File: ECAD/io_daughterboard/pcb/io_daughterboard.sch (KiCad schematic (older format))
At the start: 89 parts, among them CON1 BARREL_JACK, J1 XF2L-0625-1A, J2 4-1734839-0, P1 CONN_02X32, P10 CONN_01X06, P11 CONN_01X06, P12 CONN_01X06, P13 CONN_01X06, P14 CONN_01X06, P15 CONN_01X06, P16 CONN_01X06, P17 CONN_01X06, P18 CONN_01X06, P19 CONN_01X04, P2 CONN_02X32, P3 CONN_01X06, P4 CONN_01X06, P5 CONN_01X06, P6 CONN_01X06, P7 CONN_01X06, P8 CONN_01X06, P9 CONN_01X06, SW1 Reset Button, SW2 User Button, U1 FAN5333BSX, U10 SN74LV1T34DCKR, U11 SN74LV1T34DCKR, U2 SPX3819M5-L-3-3, U3 74HC244, U4 74HC244, U5 74HC244, U6 STMPE811QTR, U7 74HC244, U8 74HC244, U9 74HC244

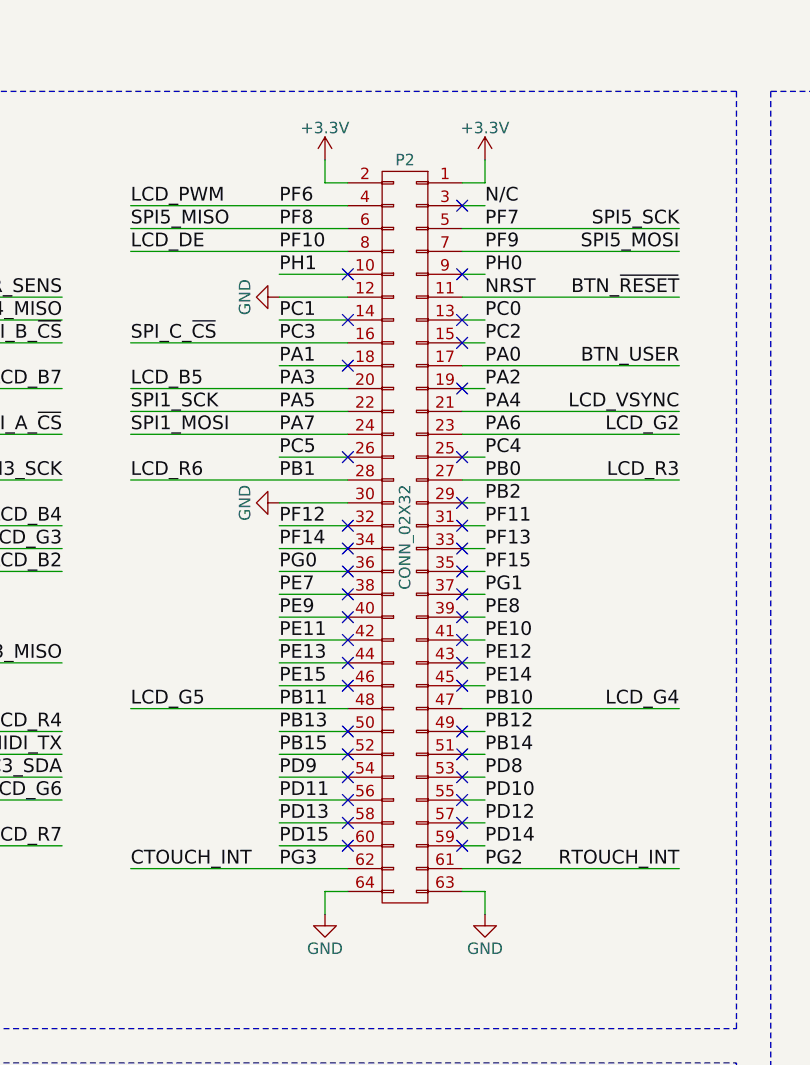
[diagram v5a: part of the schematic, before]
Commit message: Flipped board to make LCD right side up.  Regenerated netlist with footprints.
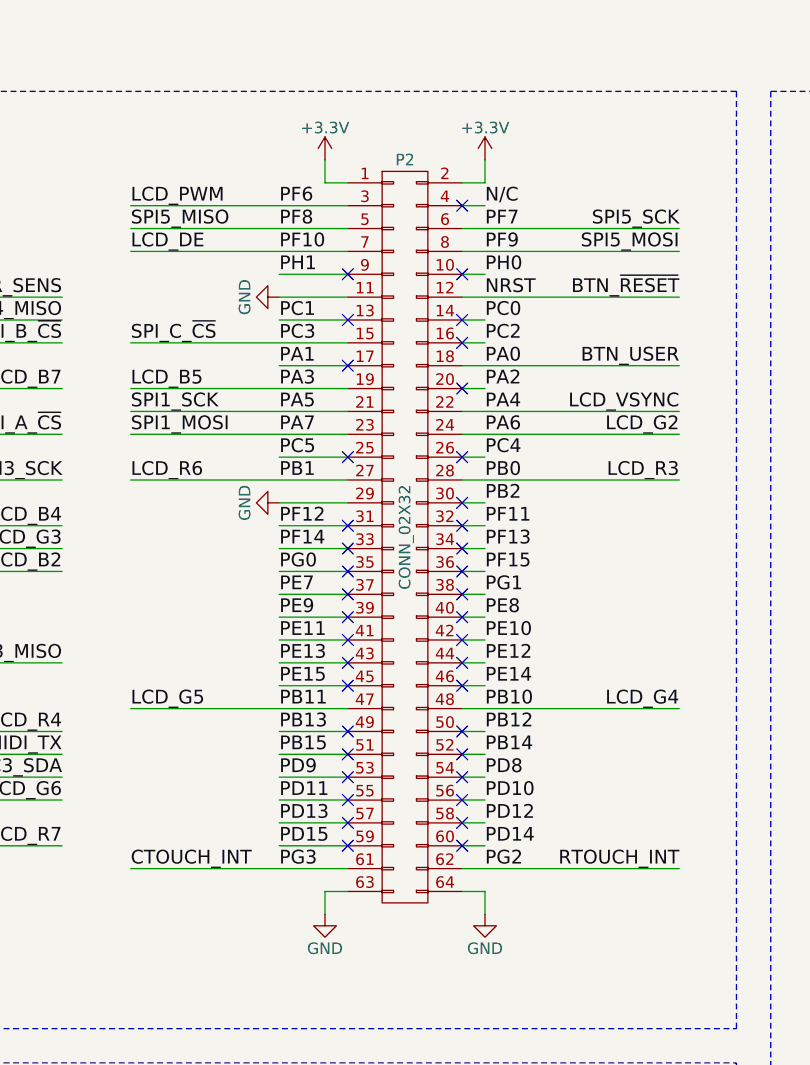
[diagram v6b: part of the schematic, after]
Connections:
- net BTN_USER: now also P2.18 (P18); no longer P2.17 (P17)
- net BTN_~RESET: now also P2.12 (P12); no longer P2.11 (P11)
- net CTOUCH_INT: now also P2.61 (P61); no longer P2.62 (P62)
- net GND: now also P2.11 (P11), P2.29 (P29); no longer P2.12 (P12), P2.30 (P30)
- net LCD_B5: now also P2.19 (P19); no longer P2.20 (P20)
- net LCD_DE: now also P2.7 (P7); no longer P2.8 (P8)
- net LCD_G2: now also P2.24 (P24); no longer P2.23 (P23)
- net LCD_G4: now also P2.48 (P48); no longer P2.47 (P47)
- net LCD_G5: now also P2.47 (P47); no longer P2.48 (P48)
- net LCD_PWM: now also P2.3 (P3); no longer P2.4 (P4)
- net LCD_R0: now also P2.27 (P27); no longer P2.28 (P28)
- net LCD_R3: now also P2.28 (P28); no longer P2.27 (P27)
- net LCD_VSYNC: now also P2.22 (P22); no longer P2.21 (P21)
- net N/C: now also P2.4 (P4); no longer P2.3 (P3)
- net PA1: now also P2.17 (P17); no longer P2.18 (P18)
- net PA2: now also P2.20 (P20); no longer P2.19 (P19)
- net PA5: now also P2.21 (P21); no longer P2.22 (P22)
- net PA7: now also P2.23 (P23); no longer P2.24 (P24)
- net PB12: now also P2.50 (P50); no longer P2.49 (P49)
- net PB13: now also P2.49 (P49); no longer P2.50 (P50)
- net PB14: now also P2.52 (P52); no longer P2.51 (P51)
- net PB15: now also P2.51 (P51); no longer P2.52 (P52)
- net PB2: now also P2.30 (P30); no longer P2.29 (P29)
- net PC0: now also P2.14 (P14); no longer P2.13 (P13)
- net PC1: now also P2.13 (P13); no longer P2.14 (P14)
- net PC2: now also P2.16 (P16); no longer P2.15 (P15)
- net PC3: now also P2.15 (P15); no longer P2.16 (P16)
- net PC4: now also P2.26 (P26); no longer P2.25 (P25)
- net PC5: now also P2.25 (P25); no longer P2.26 (P26)
- net PD10: now also P2.56 (P56); no longer P2.55 (P55)
- net PD11: now also P2.55 (P55); no longer P2.56 (P56)
- net PD12: now also P2.58 (P58); no longer P2.57 (P57)
- net PD13: now also P2.57 (P57); no longer P2.58 (P58)
- net PD14: now also P2.60 (P60); no longer P2.59 (P59)
- net PD15: now also P2.59 (P59); no longer P2.60 (P60)
- net PD8: now also P2.54 (P54); no longer P2.53 (P53)
- net PD9: now also P2.53 (P53); no longer P2.54 (P54)
- net PE10: now also P2.42 (P42); no longer P2.41 (P41)
- net PE11: now also P2.41 (P41); no longer P2.42 (P42)
- net PE12: now also P2.44 (P44); no longer P2.43 (P43)
- net PE13: now also P2.43 (P43); no longer P2.44 (P44)
- net PE14: now also P2.46 (P46); no longer P2.45 (P45)
- net PE15: now also P2.45 (P45); no longer P2.46 (P46)
- net PE7: now also P2.37 (P37); no longer P2.38 (P38)
- net PE8: now also P2.40 (P40); no longer P2.39 (P39)
- net PE9: now also P2.39 (P39); no longer P2.40 (P40)
- net PF11: now also P2.32 (P32); no longer P2.31 (P31)
- net PF12: now also P2.31 (P31); no longer P2.32 (P32)
- net PF13: now also P2.34 (P34); no longer P2.33 (P33)
- net PF14: now also P2.33 (P33); no longer P2.34 (P34)
- net PF15: now also P2.36 (P36); no longer P2.35 (P35)
- net PF7: now also P2.6 (P6); no longer P2.5 (P5)
- net PF8: now also P2.5 (P5); no longer P2.6 (P6)
- net PF9: now also P2.8 (P8); no longer P2.7 (P7)
- net PG0: now also P2.35 (P35); no longer P2.36 (P36)
- net PG1: now also P2.38 (P38); no longer P2.37 (P37)
- net PG2: now also P2.62 (P62); no longer P2.61 (P61)
- net PH0: now also P2.10 (P10); no longer P2.9 (P9)
- net PH1: now also P2.9 (P9); no longer P2.10 (P10)
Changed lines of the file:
@@
 F 3 "" H 4800 2150 50  0000 C CNN
 	1    4800 2550
-	-1   0    0    -1
+	1    0    0    -1
 $EndComp
 $Comp

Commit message: Dimensioned board for P1 and P2 connectors.  Experimenting with different slave connectors.
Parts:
- P1, P2: footprint Socket_Strips:Socket_Strip_Straight_2x32 -> daughterfeet:Socket_Strip_Reversed_2x32
- P10, P11, P12, P13, P14, P15, P16, P17, P18, P3, P4, P5, P6, P7, P8, P9: footprint daughterfeet:B6B-PH-SM4-TB -> Pin_Headers:Pin_Header_Straight_2x03_Pitch2.00mm
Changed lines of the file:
@@
 EESchema Schematic File Version 2
+LIBS:io_daughterboard-rescue
 LIBS:bored
 LIBS:power
@@
 F 0 "P1" H 2100 4200 50  0000 C CNN
 F 1 "CONN_02X32" V 2100 2550 50  0000 C CNN
-F 2 "Socket_Strips:Socket_Strip_Straight_2x32" H 2100 2150 50  0001 C CNN
+F 2 "daughterfeet:Socket_Strip_Reversed_2x32" H 2100 2150 50  0001 C CNN
 F 3 "" H 2100 2150 50  0000 C CNN
 	1    2100 2550
@@
 F 0 "P2" H 4800 4200 50  0000 C CNN
 F 1 "CONN_02X32" V 4800 2550 50  0000 C CNN
-F 2 "Socket_Strips:Socket_Strip_Straight_2x32" H 4800 2150 50  0001 C CNN
+F 2 "daughterfeet:Socket_Strip_Reversed_2x32" H 4800 2150 50  0001 C CNN
 F 3 "" H 4800 2150 50  0000 C CNN
 	1    4800 2550
@@
 F 0 "P3" H 1750 5850 50  0000 C CNN
 F 1 "CONN_01X06" V 1850 5500 50  0000 C CNN
-F 2 "daughterfeet:B6B-PH-SM4-TB" H 1750 5500 50  0001 C CNN
+F 2 "Pin_Headers:Pin_Header_Straight_2x03_Pitch2.00mm" H 1750 5500 50  0001 C CNN
 F 3 "" H 1750 5500 50  0000 C CNN
 	1    1750 5500
@@
 F 0 "P7" H 3150 5850 50  0000 C CNN
 F 1 "CONN_01X06" V 3250 5500 50  0000 C CNN
-F 2 "daughterfeet:B6B-PH-SM4-TB" H 3150 5500 50  0001 C CNN
+F 2 "Pin_Headers:Pin_Header_Straight_2x03_Pitch2.00mm" H 3150 5500 50  0001 C CNN
 F 3 "" H 3150 5500 50  0000 C CNN
 	1    3150 5500
@@
 F 0 "P11" H 4550 5850 50  0000 C CNN
 F 1 "CONN_01X06" V 4650 5500 50  0000 C CNN
-F 2 "daughterfeet:B6B-PH-SM4-TB" H 4550 5500 50  0001 C CNN
+F 2 "Pin_Headers:Pin_Header_Straight_2x03_Pitch2.00mm" H 4550 5500 50  0001 C CNN
 F 3 "" H 4550 5500 50  0000 C CNN
 	1    4550 5500
@@
 F 0 "P4" H 1750 6850 50  0000 C CNN
 F 1 "CONN_01X06" V 1850 6500 50  0000 C CNN
-F 2 "daughterfeet:B6B-PH-SM4-TB" H 1750 6500 50  0001 C CNN
+F 2 "Pin_Headers:Pin_Header_Straight_2x03_Pitch2.00mm" H 1750 6500 50  0001 C CNN
 F 3 "" H 1750 6500 50  0000 C CNN
 	1    1750 6500
@@
 F 0 "P8" H 3150 6850 50  0000 C CNN
 F 1 "CONN_01X06" V 3250 6500 50  0000 C CNN
-F 2 "daughterfeet:B6B-PH-SM4-TB" H 3150 6500 50  0001 C CNN
+F 2 "Pin_Headers:Pin_Header_Straight_2x03_Pitch2.00mm" H 3150 6500 50  0001 C CNN
 F 3 "" H 3150 6500 50  0000 C CNN
 	1    3150 6500
@@
 F 0 "P12" H 4550 6850 50  0000 C CNN
 F 1 "CONN_01X06" V 4650 6500 50  0000 C CNN
-F 2 "daughterfeet:B6B-PH-SM4-TB" H 4550 6500 50  0001 C CNN
+F 2 "Pin_Headers:Pin_Header_Straight_2x03_Pitch2.00mm" H 4550 6500 50  0001 C CNN
 F 3 "" H 4550 6500 50  0000 C CNN
 	1    4550 6500
@@
 F 0 "P15" H 5950 5850 50  0000 C CNN
 F 1 "CONN_01X06" V 6050 5500 50  0000 C CNN
-F 2 "daughterfeet:B6B-PH-SM4-TB" H 5950 5500 50  0001 C CNN
+F 2 "Pin_Headers:Pin_Header_Straight_2x03_Pitch2.00mm" H 5950 5500 50  0001 C CNN
 F 3 "" H 5950 5500 50  0000 C CNN
 	1    5950 5500
@@
 F 0 "P16" H 5950 6850 50  0000 C CNN
 F 1 "CONN_01X06" V 6050 6500 50  0000 C CNN
-F 2 "daughterfeet:B6B-PH-SM4-TB" H 5950 6500 50  0001 C CNN
+F 2 "Pin_Headers:Pin_Header_Straight_2x03_Pitch2.00mm" H 5950 6500 50  0001 C CNN
 F 3 "" H 5950 6500 50  0000 C CNN
 	1    5950 6500
@@
 F 0 "P5" H 1750 7850 50  0000 C CNN
 F 1 "CONN_01X06" V 1850 7500 50  0000 C CNN
-F 2 "daughterfeet:B6B-PH-SM4-TB" H 1750 7500 50  0001 C CNN
+F 2 "Pin_Headers:Pin_Header_Straight_2x03_Pitch2.00mm" H 1750 7500 50  0001 C CNN
 F 3 "" H 1750 7500 50  0000 C CNN
 	1    1750 7500
@@
 F 0 "P9" H 3150 7850 50  0000 C CNN
 F 1 "CONN_01X06" V 3250 7500 50  0000 C CNN
-F 2 "daughterfeet:B6B-PH-SM4-TB" H 3150 7500 50  0001 C CNN
+F 2 "Pin_Headers:Pin_Header_Straight_2x03_Pitch2.00mm" H 3150 7500 50  0001 C CNN
 F 3 "" H 3150 7500 50  0000 C CNN
 	1    3150 7500
@@
 F 0 "P13" H 4550 7850 50  0000 C CNN
 F 1 "CONN_01X06" V 4650 7500 50  0000 C CNN
-F 2 "daughterfeet:B6B-PH-SM4-TB" H 4550 7500 50  0001 C CNN
+F 2 "Pin_Headers:Pin_Header_Straight_2x03_Pitch2.00mm" H 4550 7500 50  0001 C CNN
 F 3 "" H 4550 7500 50  0000 C CNN
 	1    4550 7500
@@
 F 0 "P6" H 1750 8850 50  0000 C CNN
 F 1 "CONN_01X06" V 1850 8500 50  0000 C CNN
-F 2 "daughterfeet:B6B-PH-SM4-TB" H 1750 8500 50  0001 C CNN
+F 2 "Pin_Headers:Pin_Header_Straight_2x03_Pitch2.00mm" H 1750 8500 50  0001 C CNN
 F 3 "" H 1750 8500 50  0000 C CNN
 	1    1750 8500
@@
 F 0 "P10" H 3150 8850 50  0000 C CNN
 F 1 "CONN_01X06" V 3250 8500 50  0000 C CNN
-F 2 "daughterfeet:B6B-PH-SM4-TB" H 3150 8500 50  0001 C CNN
+F 2 "Pin_Headers:Pin_Header_Straight_2x03_Pitch2.00mm" H 3150 8500 50  0001 C CNN
 F 3 "" H 3150 8500 50  0000 C CNN
 	1    3150 8500
@@
 F 0 "P14" H 4550 8850 50  0000 C CNN
 F 1 "CONN_01X06" V 4650 8500 50  0000 C CNN
-F 2 "daughterfeet:B6B-PH-SM4-TB" H 4550 8500 50  0001 C CNN
+F 2 "Pin_Headers:Pin_Header_Straight_2x03_Pitch2.00mm" H 4550 8500 50  0001 C CNN
 F 3 "" H 4550 8500 50  0000 C CNN
 	1    4550 8500
@@
 F 0 "P17" H 5950 7850 50  0000 C CNN
 F 1 "CONN_01X06" V 6050 7500 50  0000 C CNN
-F 2 "daughterfeet:B6B-PH-SM4-TB" H 5950 7500 50  0001 C CNN
+F 2 "Pin_Headers:Pin_Header_Straight_2x03_Pitch2.00mm" H 5950 7500 50  0001 C CNN
 F 3 "" H 5950 7500 50  0000 C CNN
 	1    5950 7500
@@
 F 0 "P18" H 5950 8850 50  0000 C CNN
 F 1 "CONN_01X06" V 6050 8500 50  0000 C CNN
-F 2 "daughterfeet:B6B-PH-SM4-TB" H 5950 8500 50  0001 C CNN
+F 2 "Pin_Headers:Pin_Header_Straight_2x03_Pitch2.00mm" H 5950 8500 50  0001 C CNN
 F 3 "" H 5950 8500 50  0000 C CNN
 	1    5950 8500
